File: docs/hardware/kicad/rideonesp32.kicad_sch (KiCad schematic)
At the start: 0 parts

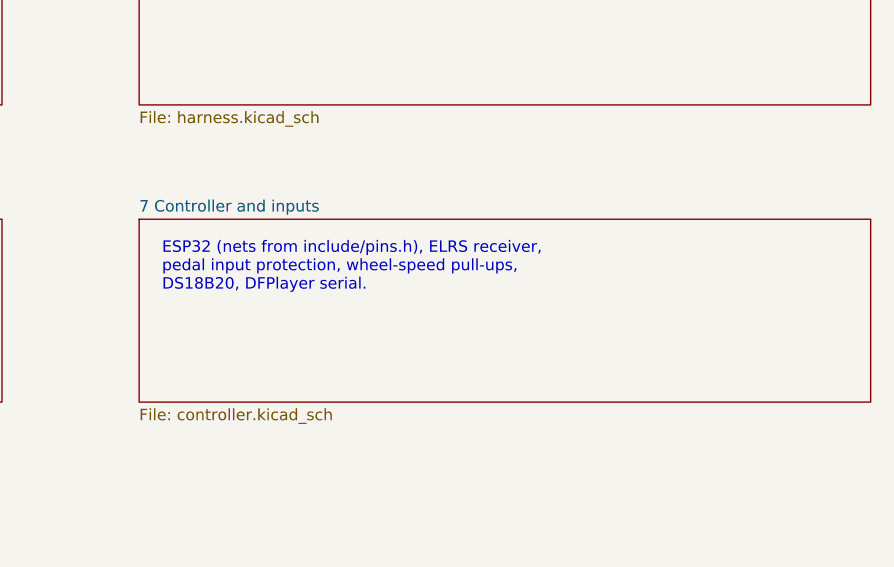
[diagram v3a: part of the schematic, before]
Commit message: Add the listen-only Bluetooth log module
An HC-06 module (U33) hears TX0, the USB serial log, through a 1k
resistor (R29); its TXD is not connected, so nothing on a phone can reach
the ESP32, whose own Wi-Fi and Bluetooth stay off. An Android phone reads
the live log with a serial terminal app.

The phone can't type, so holding the horn for 3 s with the car Locked or
Killed and stopped prints a full report: status, fault table, crash copy
and the last 50 records. `report` on the console does the same. The
trigger is in rideon_core with tests, under SR-31, plus a mutant.

New bt_setup bench firmware sets the module to 115200 baud and a PIN
before it goes in the box. Schematic, wire list, BOM, overview and the 3D
view are regenerated; BLUETOOTH.md, PINOUT, WIRING, SAFETY, README and a
phase 3 commissioning gate describe it.

Co-Authored-By: Claude Opus 5.5 <noreply@anthropic.com>
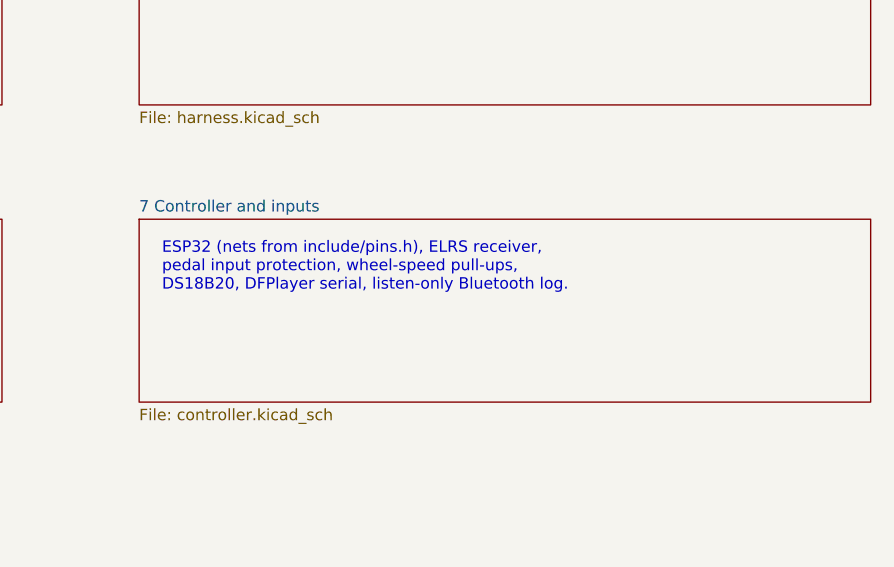
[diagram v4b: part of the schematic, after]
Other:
- note added: "ESP32 (nets from include/pins.h), ELRS receiver, pedal input protection, wheel-speed pull-ups, DS18B20, DFPlayer serial, listen-only Bluetooth log."
- note removed: "ESP32 (nets from include/pins.h), ELRS receiver, pedal input protection, wheel-speed pull-ups, DS18B20, DFPlayer serial."
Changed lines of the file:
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@@
   (instances (project "rideonesp32" (path "/e0e78d72-bf5c-51da-8e0f-d8642949b63b" (page "7"))))
 )
-(text "ESP32 (nets from include/pins.h), ELRS receiver,\npedal input protection, wheel-speed pull-ups,\nDS18B20, DFPlayer serial." (exclude_from_sim no) (at 119.38 66.04 0) (effects (font (size 1.27 1.27)) (justify left top)))
+(text "ESP32 (nets from include/pins.h), ELRS receiver,\npedal input protection, wheel-speed pull-ups,\nDS18B20, DFPlayer serial, listen-only Bluetooth log." (exclude_from_sim no) (at 119.38 66.04 0) (effects (font (size 1.27 1.27)) (justify left top)))
 (sheet (at 213.36 63.5) (size 81.28 20.32) (exclude_from_sim no) (in_bom yes) (on_board yes) (dnp no)
   (stroke (width 0.1524) (type solid)) (fill (color 0 0 0 0.0000))
